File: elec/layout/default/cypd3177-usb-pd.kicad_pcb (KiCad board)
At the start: 2 copper layers, 225.7 x 100.8 mm, 0 parts

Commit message: layout progress
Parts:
- added C1: 25V 1uF X5R ±10% 0402 Multilayer Ceramic Capacitors MLCC - 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, lib:C0402, F.Cu at (122.5, 116.5)
- added C10: 16V 100nF X7R ±10% 0402 Multilayer Ceramic Capacitors MLCC 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, lib:C0402, F.Cu at (149.2, 127.5)
- added C11: 25V 10uF X5R ±10% 0805 Multilayer Ceramic Capacitors MLCC -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, lib:C0805, F.Cu at (146.6, 107.5)
- added C12: 25V 10uF X5R ±10% 0805 Multilayer Ceramic Capacitors MLCC -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, lib:C0805, F.Cu at (146.4, 116.5)
- added C2: 25V 1uF X5R ±10% 0402 Multilayer Ceramic Capacitors MLCC - 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, lib:C0402, F.Cu at (126.5, 117.0)
- added C3: 25V 1uF X5R ±10% 0402 Multilayer Ceramic Capacitors MLCC - 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, lib:C0402, F.Cu at (117.5, 121.0)
- added C4: 16V 100nF X7R ±10% 0402 Multilayer Ceramic Capacitors MLCC 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, lib:C0402, F.Cu at (117.5, 118.0)
- added C5: 16V 100nF X7R ±10% 0402 Multilayer Ceramic Capacitors MLCC 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, lib:C0402, F.Cu at (117.5, 119.5)
- added C6: 25V 1uF X5R ±10% 0402 Multilayer Ceramic Capacitors MLCC - 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, lib:C0402, F.Cu at (117.5, 122.5)
- added C7: 10V 3.3uF X5R ±10% 0402 Multilayer Ceramic Capacitors MLCC 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, lib:C0402, F.Cu at (121.0, 116.5)
- added C8: 6.3V 10uF X5R ±20% 0402 Multilayer Ceramic Capacitors MLCC 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, lib:C0402, F.Cu at (149.4, 122.7)
- added C9: 25V 10uF X5R ±10% 0805 Multilayer Ceramic Capacitors MLCC -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, lib:C0805, F.Cu at (145.7, 122.8)
- added DS1: , lib:SOD-323_L1.8-W1.3-LS2.5-RD, F.Cu at (149.6, 128.8)
- added DZ1: , lib:SOD-123_L2.7-W1.7-LS3.8-RD, F.Cu at (126.5, 111.0)
- added L1: , lib:IND-SMD_L4.0-W4.0, F.Cu at (145.3, 126.5)
- added LED1: , lib:LED0603-RD, F.Cu at (130.5, 126.0)
- added R1: 62.5mW Thick Film Resistors 50V ±100ppm/℃ ±1% 10kΩ 0402 Chi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, lib:R0402, F.Cu at (119.5, 116.5)
- added R10: 62.5mW Thick Film Resistors ±100ppm/℃ ±1% 316Ω 0402 Chip Re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, lib:R0402, F.Cu at (119.5, 126.5)
- added R11: 62.5mW Thick Film Resistors 50V ±100ppm/℃ ±1% 54.9Ω 0402 Ch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, lib:R0402, F.Cu at (119.5, 129.0)
- added R12: 62.5mW Thick Film Resistors 50V ±100ppm/℃ ±1% 36.5Ω 0402 Ch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, lib:R0402, F.Cu at (121.5, 126.5)
- added R13: 62.5mW Thick Film Resistors 50V ±100ppm/℃ ±1% 300Ω 0402 Chi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, lib:R0402, F.Cu at (121.5, 129.0)
- added R14: 62.5mW Thick Film Resistors 50V ±100ppm/℃ ±1% 36.5Ω 0402 Ch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, lib:R0402, F.Cu at (123.3, 126.5)
- added R15: 62.5mW Thick Film Resistors 50V ±100ppm/℃ ±1% 300Ω 0402 Chi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, lib:R0402, F.Cu at (123.3, 129.0)
- added R16: 62.5mW Thick Film Resistors 50V ±100ppm/℃ ±1% 383Ω 0402 Chi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, lib:R0402, F.Cu at (125.0, 126.5)
- added R17: 62.5mW Thick Film Resistors 50V ±800ppm/℃ ±1% 0Ω 0402 Chip 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, lib:R0402, F.Cu at (125.0, 129.0)
- added R18: 62.5mW Thick Film Resistors 50V ±100ppm/℃ ±1% 23.7kΩ 0402 C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, lib:R0402, F.Cu at (146.9, 121.3)
- added R19: 62.5mW Thick Film Resistors 50V ±100ppm/℃ ±1% 4.3kΩ 0402 Ch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, lib:R0402, F.Cu at (144.9, 121.3)
- added R2: 62.5mW Thick Film Resistors 50V ±100ppm/℃ ±1% 1kΩ 0402 Chip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, lib:R0402, F.Cu at (126.5, 114.5)
- added R20: 125mW Thick Film Resistors 150V ±800ppm/℃ ±1% 0Ω 0805 Chip 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, lib:R0805, F.Cu at (136.5, 125.0)
- added R3: 100mW Thick Film Resistors 75V ±100ppm/℃ ±1% 47kΩ 0603 Chip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, lib:R0603, F.Cu at (134.5, 113.8)
- added R4: 62.5mW Thick Film Resistors 50V ±100ppm/℃ ±1% 51kΩ 0402 Chi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, lib:R0402, F.Cu at (129.0, 123.0)
- added R5: 62.5mW Thick Film Resistors 50V ±100ppm/℃ ±1% 1kΩ 0402 Chip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, lib:R0402, F.Cu at (131.8, 123.0)
- added R6: 62.5mW Thick Film Resistors 50V ±100ppm/℃ ±1% 4.7kΩ 0402 Ch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, lib:R0402, F.Cu at (126.3, 122.5)
- added R7: 62.5mW Thick Film Resistors 50V ±100ppm/℃ ±1% 10kΩ 0402 Chi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, lib:R0402, F.Cu at (143.5, 103.5)
- added R8: 62.5mW Thick Film Resistors 50V ±100ppm/℃ ±1% 10kΩ 0402 Chi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, lib:R0402, F.Cu at (146.0, 103.5)
- added R9: 62.5mW Thick Film Resistors ±100ppm/℃ ±0.5% 1.78kΩ 0402 Chi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, lib:R0402, F.Cu at (128.0, 126.0)
- added U1: , lib:USB-C-SMD_KH-TYPE-C-16P, F.Cu at (125.0, 102.6)
- added U2: , lib:TQFN-24_L4.0-W4.0-P0.50-TL-EP2.8, F.Cu at (122.5, 120.8)
- added U3: , lib:SOP-8_L4.9-W3.9-P1.27-LS6.0-BL, F.Cu at (130.5, 114.0)
- added U4: , lib:SOT-23_L2.9-W1.3-P1.90-LS2.4-BR, F.Cu at (128.3, 120.0)
- added U5: , lib:SOT-23_L2.9-W1.3-P1.90-LS2.4-BR, F.Cu at (132.5, 120.0)
- added U6: , lib:SOT-323-3_L2.0-W1.3-P1.30-LS2.1-BR, F.Cu at (128.0, 128.5)
- added U7: , lib:SOT-23-6_L2.9-W1.6-P0.95-LS2.8-BR, F.Cu at (149.8, 125.2)
- added U8: , lib:SOT-223-3_L6.5-W3.4-P2.30-LS7.0-BR, F.Cu at (146.5, 112.0)
- added U9: , lib:HDR-TH_6P-P2.54-V-M-1, F.Cu at (139.7, 100.5)
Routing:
- net usb_c-vcc: track 0.00 -> 50.1 mm, vias 0 -> 3
- net vcc: track 0.00 -> 45.5 mm, vias 0 -> 2
- net scl: track 0.00 -> 37.6 mm, vias 0 -> 1
- net sda: track 0.00 -> 35.0 mm, vias 0 -> 1
- net vcc-1: track 0.00 -> 32.3 mm
- net vcc-2: track 0.00 -> 31.1 mm
- net usb_c-gnd: track 0.00 -> 23.5 mm, vias 0 -> 4
- net usb_pd_device.cypd3177_ic-vcc-1: track 0.00 -> 18.9 mm, vias 0 -> 5
- net cc1: track 0.00 -> 15.5 mm
- net cc2: track 0.00 -> 14.9 mm, vias 0 -> 2
- net vbus_fet_en: track 0.00 -> 12.2 mm, vias 0 -> 2
- net safe_pwr_en: track 0.00 -> 11.5 mm, vias 0 -> 2
- net usb_pd_device.load_switch.load_switch_mosfet-gnd: track 0.00 -> 11.2 mm
- net source1: track 0.00 -> 8.44 mm
- net out: track 0.00 -> 8.33 mm, vias 0 -> 2
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- added copper zone on F.Cu, net sw
- added copper zone on F.Cu, net vcc
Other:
- board size 225.7 x 100.8 mm -> 40 x 40 mm

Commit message: add complete layout
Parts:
- moved R3 5.34 mm to (131.8, 109.2), turned to 180 degrees
- moved R20 3.50 mm to (140.0, 125.0)
- moved R6 0.72 mm to (127.0, 122.5)
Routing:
- net usb_pd_device.cypd3177_ic-vcc-1: track 18.9 -> 56.4 mm, vias 5 -> 7
- net usb_pd_device.load_switch.load_switch_mosfet-gnd: track 11.2 -> 27.0 mm, vias 0 -> 2
- net usb_pd_device-vcc: track 0.00 -> 9.93 mm
- net usb_c-gnd: track 23.5 -> 29.5 mm, vias 4 -> 17
- net vcc-1: track 32.3 -> 36.7 mm
- net source1: track 8.44 -> 12.1 mm
- net hpi_int: track 0.00 -> 1.66 mm, vias 0 -> 1
- net flip: track 2.56 -> 3.12 mm
- added copper zone on B.Cu, net usb_c-gnd
- added copper zone on F.Cu, net usb_c-gnd
- added copper zone on F.Cu, net vcc-1

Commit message: fix for production
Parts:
- R20: value 125mW Thick Film Resistors 150V ±800ppm/℃ ±1% 0Ω 0805 Chip Resistor - Surface Mount ROHS -> 0 ohm
- moved C1 0.60 mm to (121.9, 116.5)
- moved C7 0.60 mm to (120.4, 116.5)
- moved R1 0.60 mm to (118.9, 116.5)
- moved U9 0.20 mm to (139.7, 100.7)
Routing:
- net usb_c-vcc: track 50.1 -> 58.5 mm
- net vcc-2: track 31.1 -> 24.1 mm
- net vcc-1: track 36.7 -> 40.2 mm, vias 0 -> 3
- net source1: track 12.1 -> 12.7 mm
- net vcc: track 45.5 -> 45.4 mm, vias 2 -> 0
- net usb_c-gnd: vias 17 -> 48

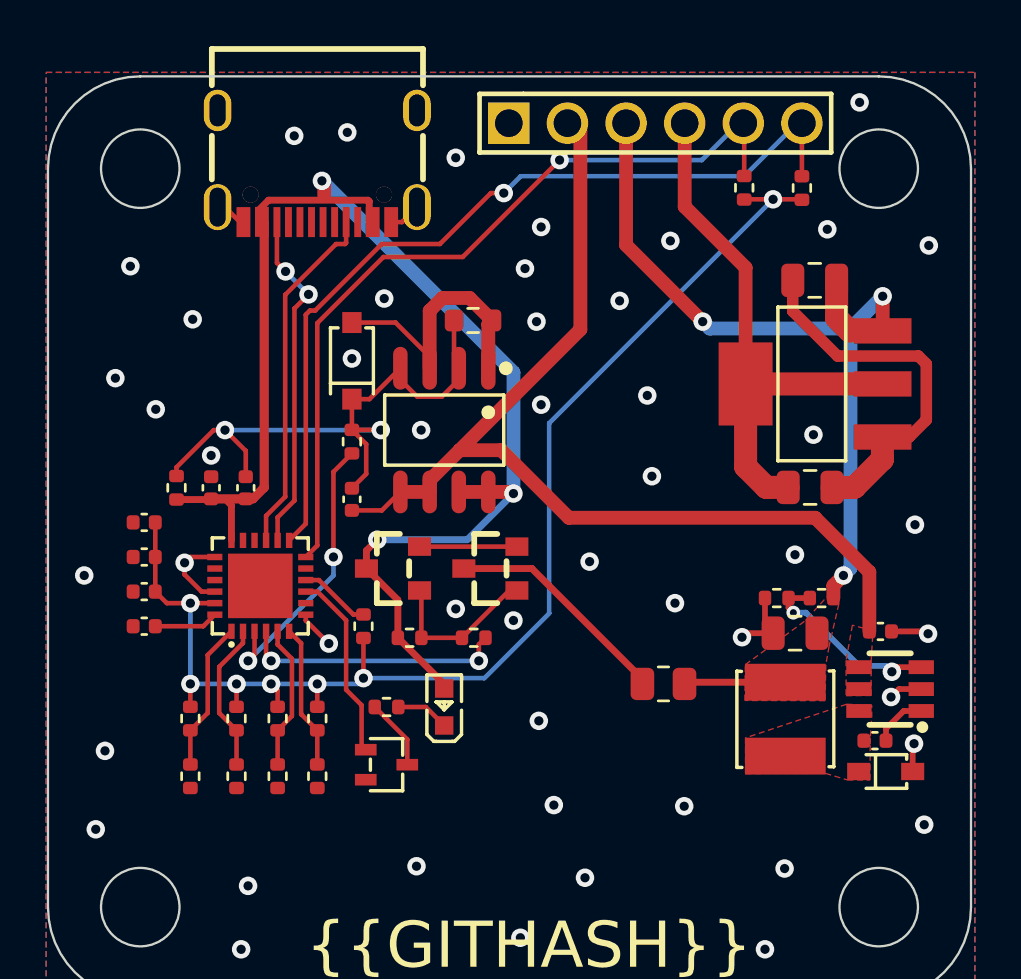
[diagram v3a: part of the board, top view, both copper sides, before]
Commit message: add fields
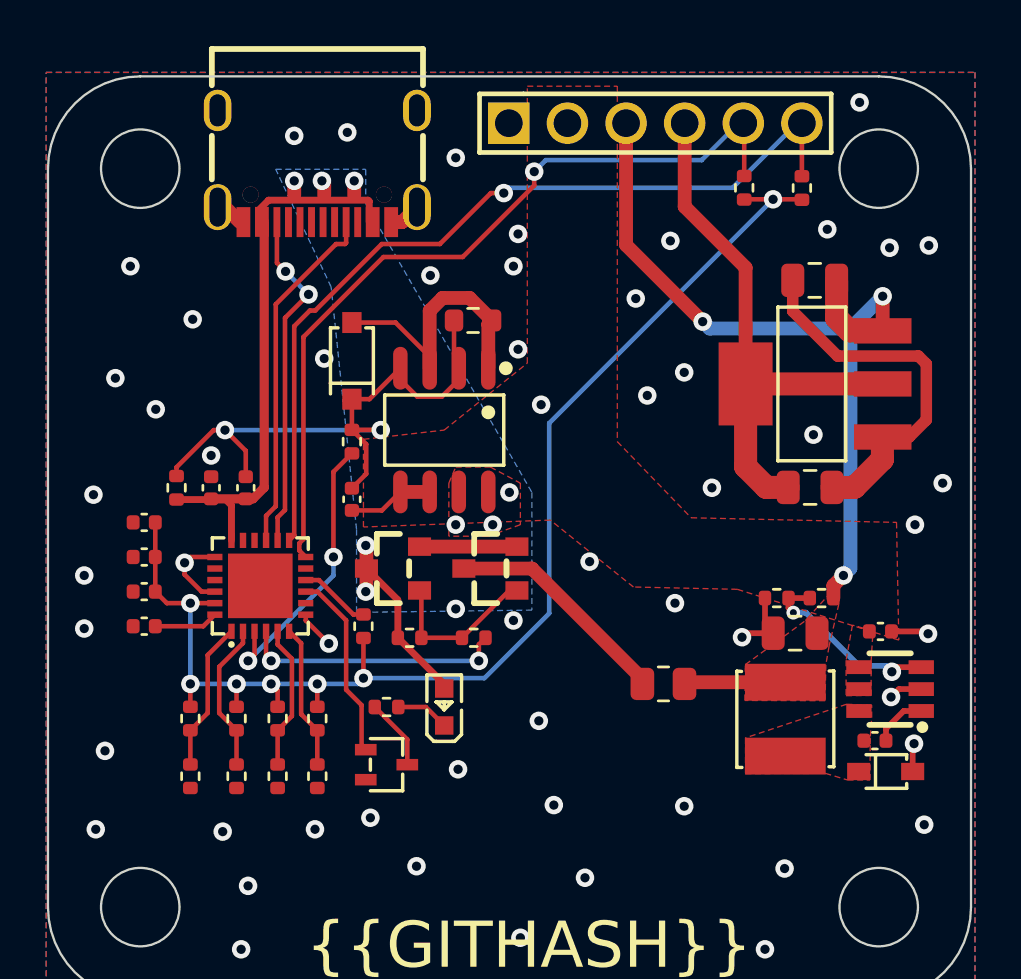
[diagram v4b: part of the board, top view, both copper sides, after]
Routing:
- net vcc: track 45.4 -> 3.81 mm
- net usb_c-vcc: track 58.5 -> 34.3 mm, vias 3 -> 8
- net sda: track 35.0 -> 35.6 mm
- net usb_c-gnd: vias 48 -> 55
- added copper zone on B.Cu, net usb_c-vcc
- added copper zone on F.Cu, net usb_c-vcc
